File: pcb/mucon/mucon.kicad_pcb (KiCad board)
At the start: 2 copper layers, 23 x 23 mm, 27 parts, among them IC1 MDBT50Q-1M, J1 Conn_01x08, SW1 SW_PUSH, SW2 SW_PUSH, SW3 SW_PUSH, SW4 SW_PUSH, SW5 SW_PUSH, Y1 32.768kHz

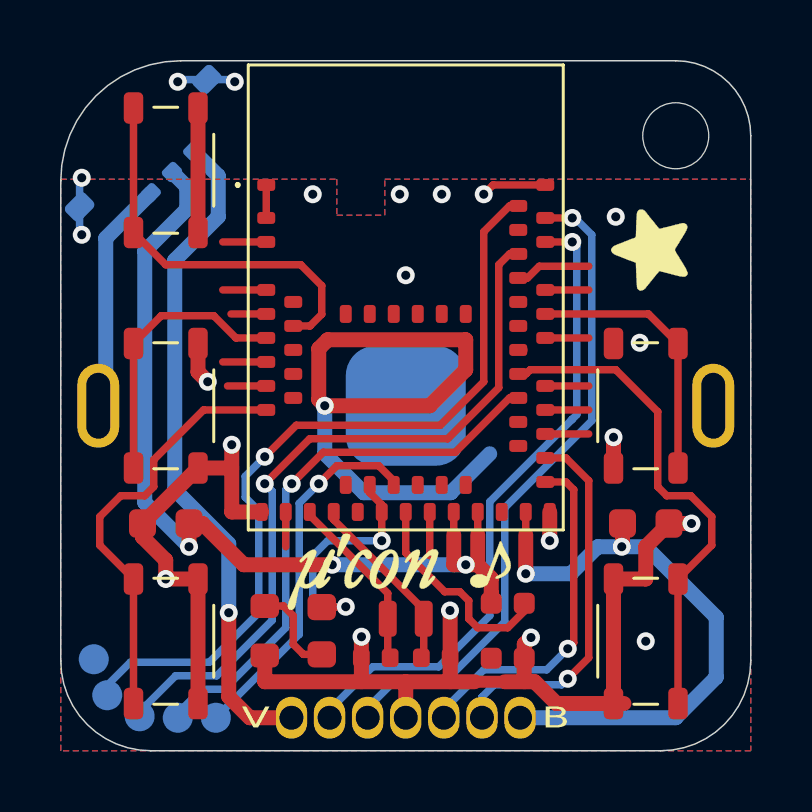
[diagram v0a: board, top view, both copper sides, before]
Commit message: change capacitor (from 1uF to 100uF), PCB design files are in KiCad6 format
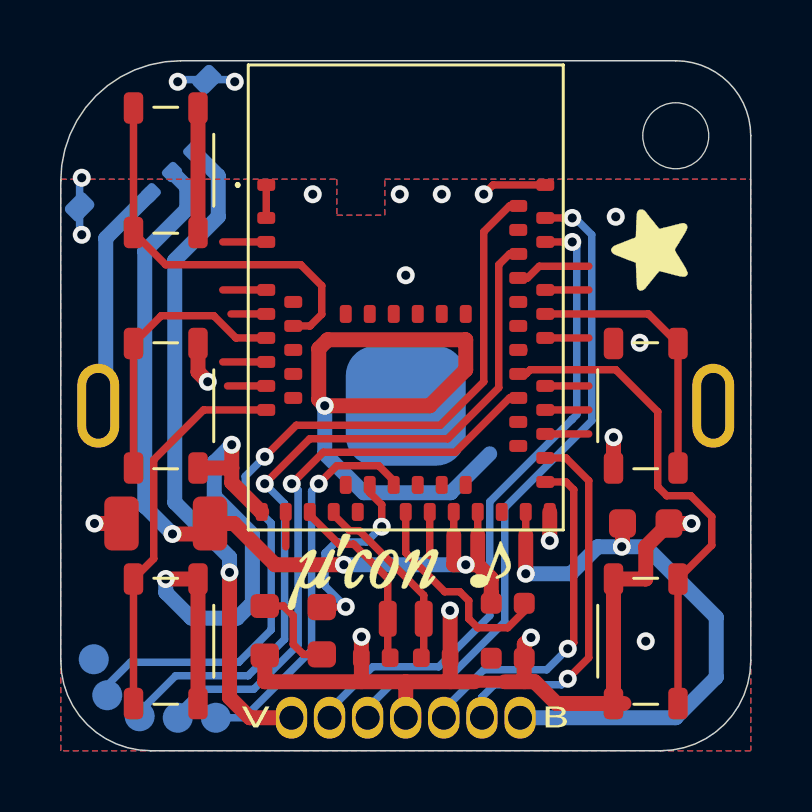
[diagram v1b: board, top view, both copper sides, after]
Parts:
- C1: value 4.7uF -> 1uF
- C2: value 1uF -> 100uF; footprint Capacitor_SMD:C_0603_1608Metric -> Capacitor_SMD:C_1206_3216Metric
- C3, C4: value 12p -> 9p
- Y1: value 32.768kHz -> 32.768kHz 9pF
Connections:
- IC1 pad 10: Net-(IC1-Pad10) -> unconnected-(IC1-Pad10)
- IC1 pad 11: Net-(IC1-Pad11) -> unconnected-(IC1-Pad11)
- IC1 pad 12: Net-(IC1-Pad12) -> unconnected-(IC1-Pad12)
- IC1 pad 13: Net-(IC1-Pad13) -> unconnected-(IC1-Pad13)
- IC1 pad 16: Net-(IC1-Pad16) -> unconnected-(IC1-Pad16)
- IC1 pad 19: Net-(IC1-Pad19) -> unconnected-(IC1-Pad19)
- IC1 pad 20: Net-(IC1-Pad20) -> unconnected-(IC1-Pad20)
- IC1 pad 25: Net-(IC1-Pad25) -> unconnected-(IC1-Pad25)
- IC1 pad 26: Net-(IC1-Pad26) -> unconnected-(IC1-Pad26)
- IC1 pad 27: Net-(IC1-Pad27) -> unconnected-(IC1-Pad27)
- IC1 pad 29: Net-(IC1-Pad29) -> unconnected-(IC1-Pad29)
- IC1 pad 3: Net-(IC1-Pad3) -> unconnected-(IC1-Pad3)
- IC1 pad 31: Net-(IC1-Pad31) -> unconnected-(IC1-Pad31)
- IC1 pad 36: Net-(IC1-Pad36) -> unconnected-(IC1-Pad36)
- IC1 pad 37: Net-(IC1-Pad37) -> unconnected-(IC1-Pad37)
- IC1 pad 38: Net-(IC1-Pad38) -> unconnected-(IC1-Pad38)
- IC1 pad 39: Net-(IC1-Pad39) -> unconnected-(IC1-Pad39)
- IC1 pad 4: Net-(IC1-Pad4) -> unconnected-(IC1-Pad4)
- IC1 pad 41: Net-(IC1-Pad41) -> unconnected-(IC1-Pad41)
- IC1 pad 43: Net-(IC1-Pad43) -> unconnected-(IC1-Pad43)
- IC1 pad 44: Net-(IC1-Pad44) -> unconnected-(IC1-Pad44)
- IC1 pad 45: Net-(IC1-Pad45) -> unconnected-(IC1-Pad45)
- IC1 pad 47: Net-(IC1-Pad47) -> unconnected-(IC1-Pad47)
- IC1 pad 48: Net-(IC1-Pad48) -> unconnected-(IC1-Pad48)
- IC1 pad 49: Net-(IC1-Pad49) -> unconnected-(IC1-Pad49)
- IC1 pad 5: Net-(IC1-Pad5) -> unconnected-(IC1-Pad5)
- IC1 pad 52: Net-(IC1-Pad52) -> unconnected-(IC1-Pad52)
- IC1 pad 56: Net-(IC1-Pad56) -> unconnected-(IC1-Pad56)
- IC1 pad 57: Net-(IC1-Pad57) -> unconnected-(IC1-Pad57)
- IC1 pad 58: Net-(IC1-Pad58) -> unconnected-(IC1-Pad58)
- IC1 pad 59: Net-(IC1-Pad59) -> unconnected-(IC1-Pad59)
- IC1 pad 6: Net-(IC1-Pad6) -> unconnected-(IC1-Pad6)
- IC1 pad 60: Net-(IC1-Pad60) -> unconnected-(IC1-Pad60)
- IC1 pad 61: Net-(IC1-Pad61) -> unconnected-(IC1-Pad61)
- IC1 pad 9: Net-(IC1-Pad9) -> unconnected-(IC1-Pad9)
- LED1 pad 1: Net-(LED1-Pad1) -> unconnected-(LED1-Pad1)
- S1 pad MP1: Net-(S1-PadMP1) -> unconnected-(S1-PadMP1)
- S1 pad MP2: Net-(S1-PadMP2) -> unconnected-(S1-PadMP2)
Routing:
- net GND: track 74.5 -> 80.0 mm, vias 18 -> 19
- net unconnected-(IC1-Pad49): track 0.00 -> 2.51 mm
- net Net-(IC1-Pad49): track 2.51 -> 0.00 mm
- net unconnected-(S1-PadMP1): track 0.00 -> 1.96 mm, vias 0 -> 2
- net unconnected-(S1-PadMP2): track 0.00 -> 1.96 mm, vias 0 -> 2
- net Net-(S1-PadMP2): track 1.96 -> 0.00 mm, vias 2 -> 0
- net Net-(S1-PadMP1): track 1.96 -> 0.00 mm, vias 2 -> 0
- net unconnected-(IC1-Pad26): track 0.00 -> 1.46 mm
- net Net-(IC1-Pad26): track 1.46 -> 0.00 mm
- net unconnected-(IC1-Pad4): track 0.00 -> 1.45 mm
- net unconnected-(IC1-Pad3): track 0.00 -> 1.45 mm
- net unconnected-(IC1-Pad10): track 0.00 -> 1.45 mm
- net Net-(IC1-Pad4): track 1.45 -> 0.00 mm
- net Net-(IC1-Pad3): track 1.45 -> 0.00 mm
- net Net-(IC1-Pad10): track 1.45 -> 0.00 mm
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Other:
- net class Default removed
- net class Power removed
